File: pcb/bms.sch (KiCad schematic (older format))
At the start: 16 parts

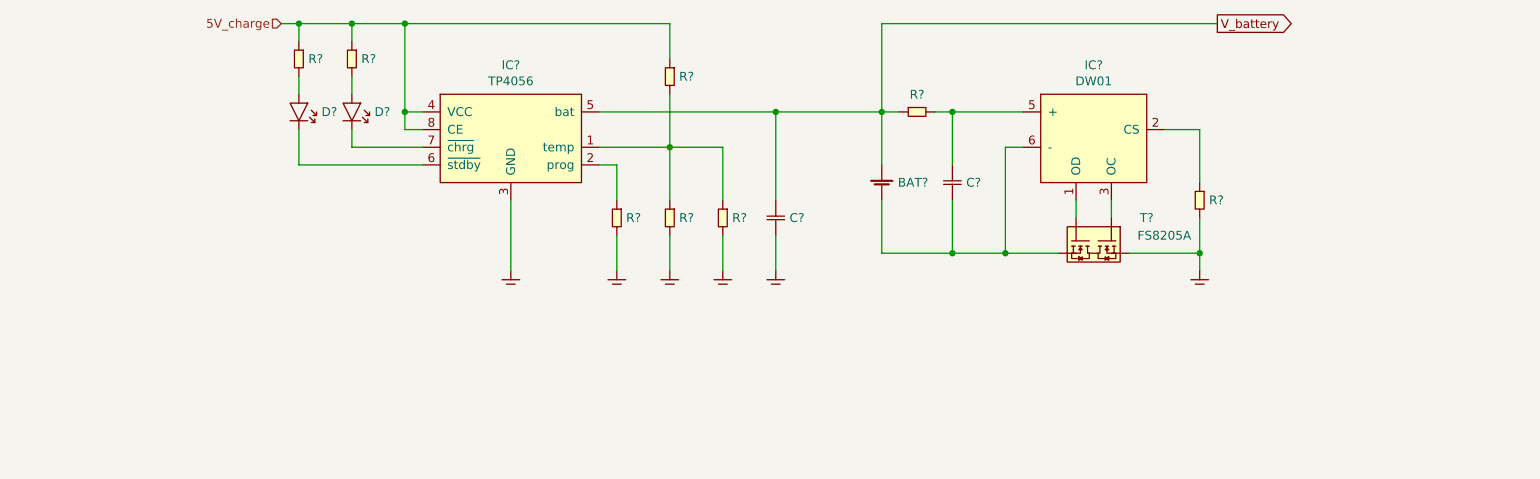
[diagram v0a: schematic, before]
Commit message: added 5V psu and battery voltage to ADC
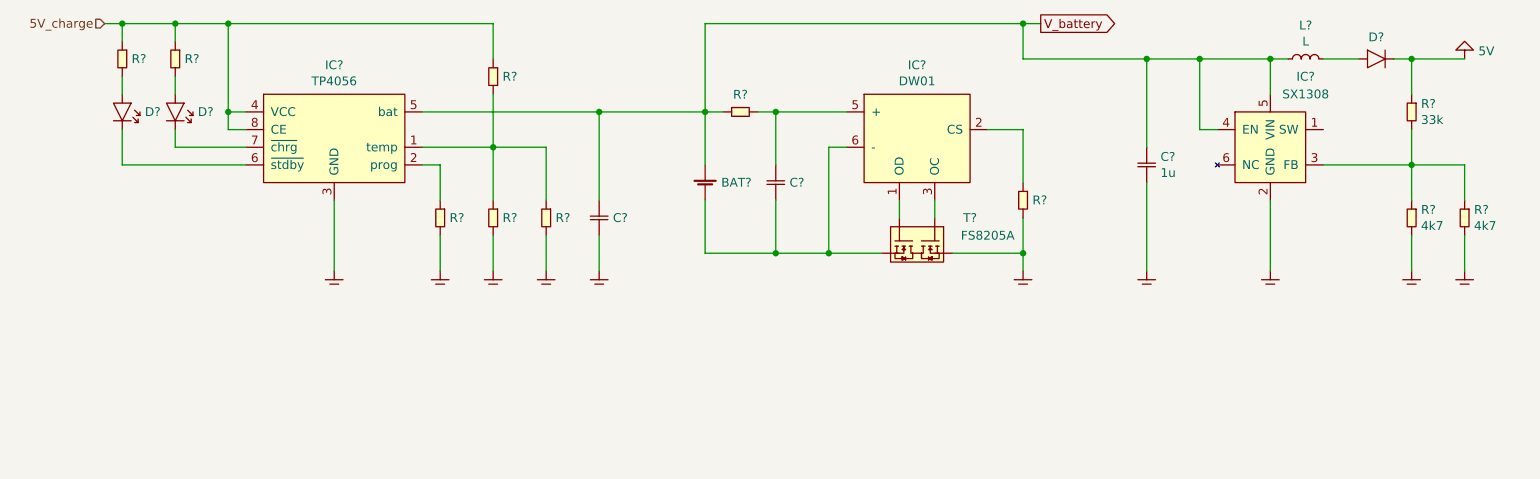
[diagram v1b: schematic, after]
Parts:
- added 5V?: 5V, symbol generic:5V
- added C?: 1u, SMT:0603, symbol generic:C
- added D?: D, SMT:0603, symbol generic:D
- added GND? (x4): GND, symbol generic:GND
- added IC?: SX1308, symbol Power:SX1308
- added L?: L, symbol generic:L
- added R?: 33k, SMT:0603, symbol generic:R
- added R? (x2): 4k7, SMT:0603, symbol generic:R
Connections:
- net GND: now also 5V?.~ (GND), C?.2, D?.2 (K), GND?.~ (GND), GND?.~ (GND), GND?.~ (GND), GND?.~ (GND), IC?.2 (GND), R?.1, R?.2, R?.2
- net V_battery: now also C?.1, IC?.4 (EN), IC?.5 (VIN), L?.1
- new net: IC?.3 (FB), R?.1, R?.1, R?.2
- new net: D?.1 (A), L?.2
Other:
- moved on the sheet: BAT?, C?, D?, IC?, R?, T?

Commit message: added 3V3 regulator
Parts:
- added 3V3?: 3V3, symbol generic:3V3
- added 5V?: 5V, symbol generic:5V
- added GND?: GND, symbol generic:GND
- added IC?: AMS1117-3.3, SOT:SOT-223, symbol Power:AMS1117-3.3
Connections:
- net GND: now also 3V3?.~ (GND), 5V?.~ (GND), GND?.~ (GND), IC?.1 (GND), IC?.2 (Vout), IC?.3 (Vin)
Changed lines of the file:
@@
 Wire Wire Line
 	9700 4600 9700 4400
+$Comp
+L Power:AMS1117-3.3 IC?
+U 1 1 5EB6EC93
+P 9400 5300
+F 0 "IC?" H 9400 5525 50  0000 C CNN
+F 1 "AMS1117-3.3" H 9400 5434 50  0000 C CNN
+F 2 "SOT:SOT-223" H 9300 5450 50  0001 C CNN
+F 3 "" H 9400 5300 50  0001 C CNN
+	1    9400 5300
+	1    0    0    -1
+$EndComp
+$Comp
+L generic:5V 5V?
+U 1 1 5EB6ED75
+P 8900 5200
+F 0 "5V?" H 9050 5250 50  0001 C CNN
+F 1 "5V" H 8978 5244 50  0000 L CNN
+F 2 "" H 8900 5200 50  0001 C CNN
+F 3 "" H 8900 5200 50  0001 C CNN
+	1    8900 5200
+	1    0    0    -1
+$EndComp
+Wire Wire Line
+	8900 5200 8900 5300
+Wire Wire Line
+	8900 5300 9200 5300
+$Comp
+L generic:GND GND?
+U 1 1 5EB705DB
+P 9400 5600
+F 0 "GND?" H 9550 5650 50  0001 C CNN
+F 1 "GND" H 9550 5600 50  0001 C CNN
+F 2 "" H 9400 5600 50  0001 C CNN
+F 3 "" H 9400 5600 50  0001 C CNN
+	1    9400 5600
+	1    0    0    -1
+$EndComp
+Wire Wire Line
+	9400 5600 9400 5500
+$Comp
+L generic:3V3 3V3?
+U 1 1 5EB71E58
+P 9800 5200
+F 0 "3V3?" H 9950 5250 50  0001 C CNN
+F 1 "3V3" H 9878 5244 50  0000 L CNN
+F 2 "" H 9800 5200 50  0001 C CNN
+F 3 "" H 9800 5200 50  0001 C CNN
+	1    9800 5200
+	1    0    0    -1
+$EndComp
+Wire Wire Line
+	9600 5300 9800 5300
+Wire Wire Line
+	9800 5300 9800 5200
 $EndSCHEMATC

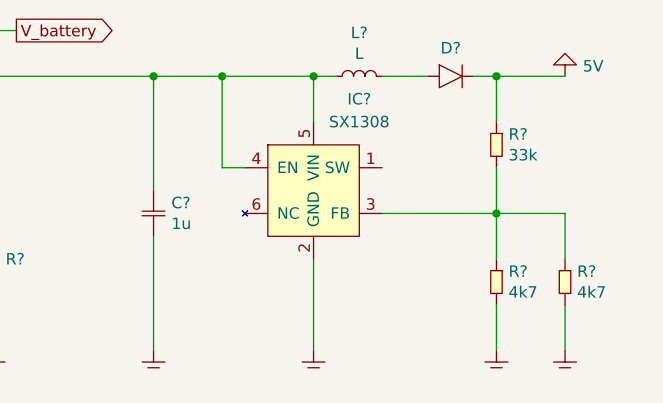
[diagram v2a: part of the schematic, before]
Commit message: added usb interface, switching signal to boost circuits
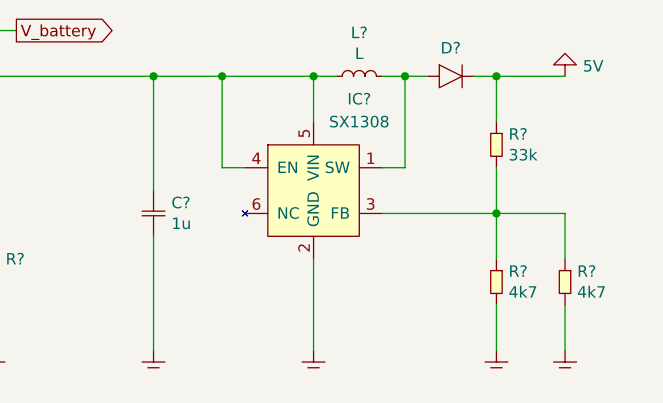
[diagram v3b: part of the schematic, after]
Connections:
- net at IC?.1 (SW): now also D?.1 (A), L?.2
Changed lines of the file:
@@
 $Descr A4 11693 8268
 encoding utf-8
-Sheet 4 4
+Sheet 4 5
 Title ""
 Date ""
@@
 $EndComp
 Wire Wire Line
-	8900 3400 9100 3400
+	8900 3400 9000 3400
 Wire Wire Line
 	8700 3400 8600 3400
@@
 Wire Wire Line
 	9800 5300 9800 5200
+Wire Wire Line
+	8900 3800 9000 3800
+Wire Wire Line
+	9000 3800 9000 3400
+Connection ~ 9000 3400
+Wire Wire Line
+	9000 3400 9100 3400
 $EndSCHEMATC
